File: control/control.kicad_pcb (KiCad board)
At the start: 2 copper layers, 100 x 40 mm, 63 parts, among them CON1 USB-MICRO-B, IC1 AD8542, IC2 STM32F072CBT6, IC3 ADP3335, IC4 AD8495, IC5 NCP1117, P1 SWD, P2 CONN_02X04, P3 CONN_01X02, U1 ROTENC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

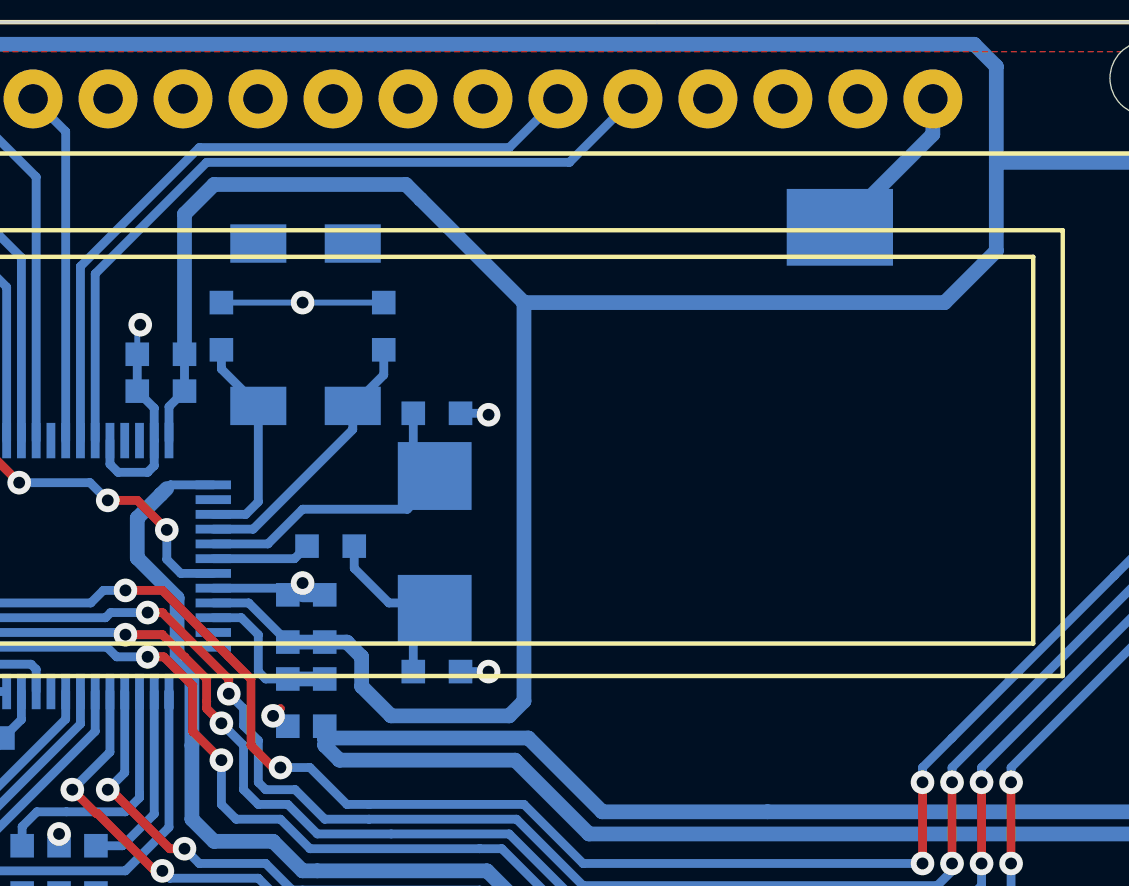
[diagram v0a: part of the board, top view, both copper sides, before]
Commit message: smaller 32k xtal, closes #21
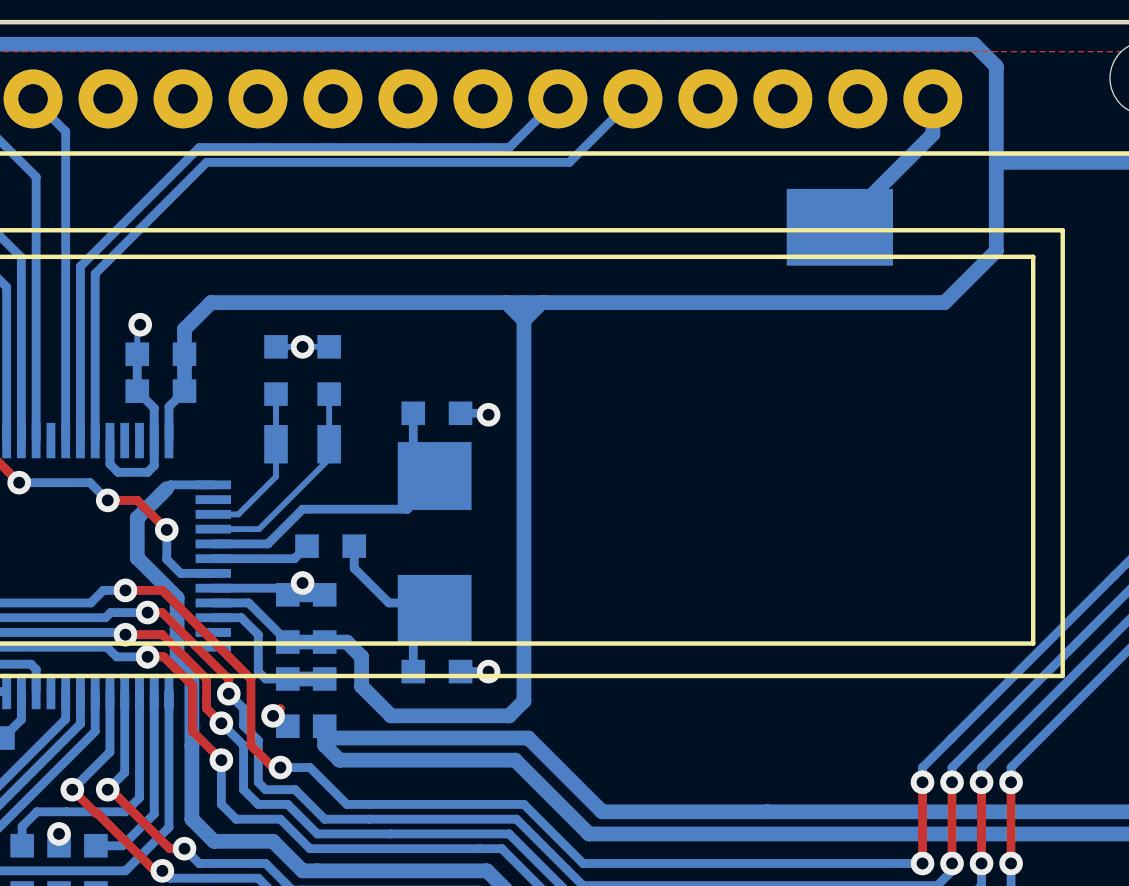
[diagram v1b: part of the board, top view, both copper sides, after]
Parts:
- X1: footprint control:SMD_XTAL_8038 -> control:R0805
- moved C11 2.38 mm to (93.1, 111.0)
- moved C12 2.38 mm to (94.9, 111.0)
- moved X1 1.43 mm to (93.1, 114.3), turned to 0 degrees
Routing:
- net VDD: track 301.8 -> 298.0 mm
- net GND: track 71.9 -> 68.2 mm
- net Net-(C12-Pad2): track 9.26 -> 7.11 mm
- net Net-(C11-Pad2): track 7.37 -> 5.45 mm

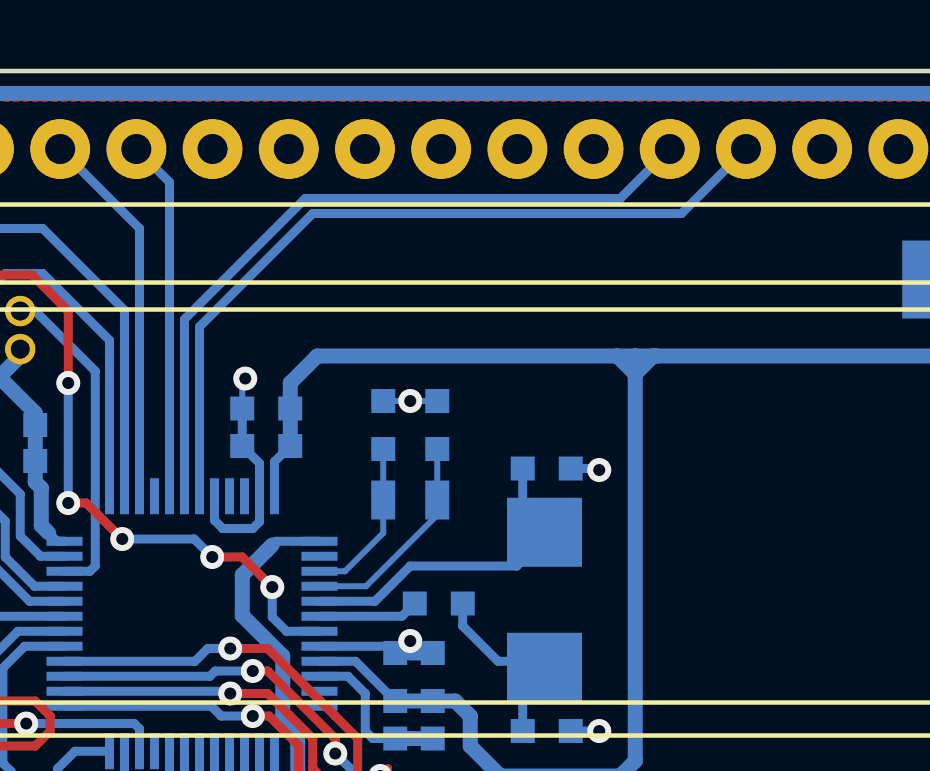
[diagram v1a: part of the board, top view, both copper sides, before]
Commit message: add LEDs to control, closes #22
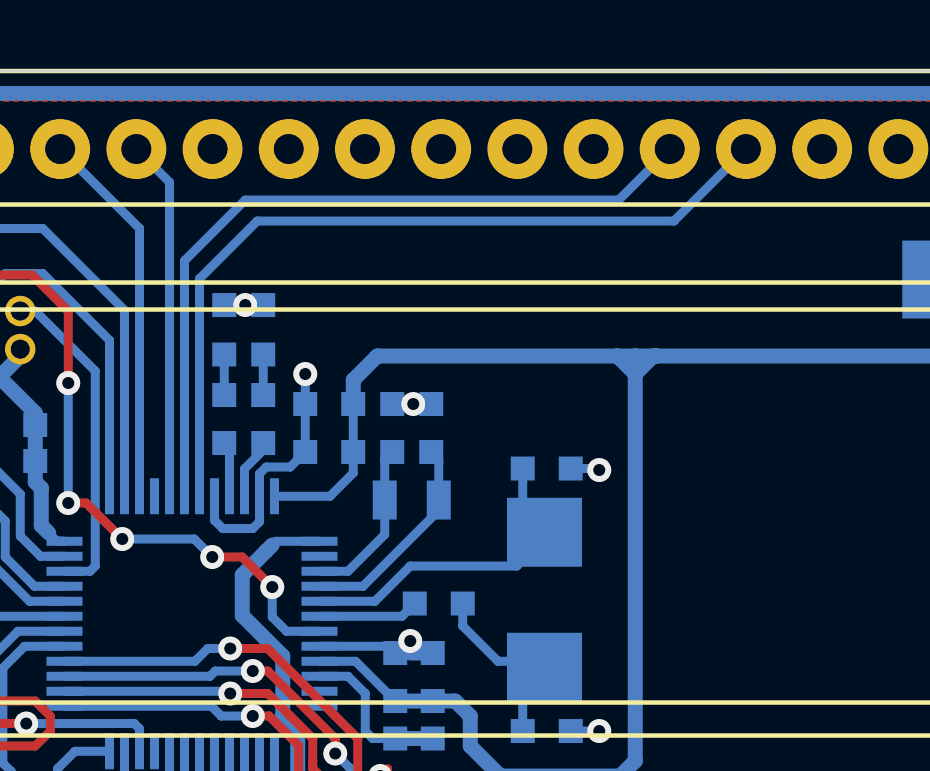
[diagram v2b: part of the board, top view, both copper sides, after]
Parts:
- added D3: GRN, control:LED0603, B.Cu at (87.8, 107.8)
- added D4: BLU, control:LED0603, B.Cu at (89.1, 107.8)
- added R13: 1k, control:R0603, B.Cu at (87.8, 110.8)
- added R14: 1k, control:R0603, B.Cu at (89.1, 110.8)
- moved C7 2.11 mm to (92.1, 112.7)
- moved C4 2.11 mm to (92.1, 111.1)
- moved C11 0.32 mm to (93.4, 111.1)
- moved C12 0.22 mm to (94.7, 111.1)
- moved X1 0.05 mm to (93.2, 114.3)
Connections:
- IC2 pad 45: (no net) -> Net-(IC2-Pad45)
- IC2 pad 46: (no net) -> Net-(IC2-Pad46)
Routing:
- net Net-(IC2-Pad46): track 0.00 -> 2.03 mm
- net Net-(IC2-Pad45): track 0.00 -> 1.85 mm
- net GND: track 68.2 -> 69.9 mm, vias 21 -> 22
- net Net-(D4-Pad2): track 0.00 -> 1.35 mm
- net Net-(D3-Pad2): track 0.00 -> 1.35 mm
- net /~OLED_CS: track 24.4 -> 25.6 mm
- net /~OLED_RST: track 26.3 -> 27.3 mm

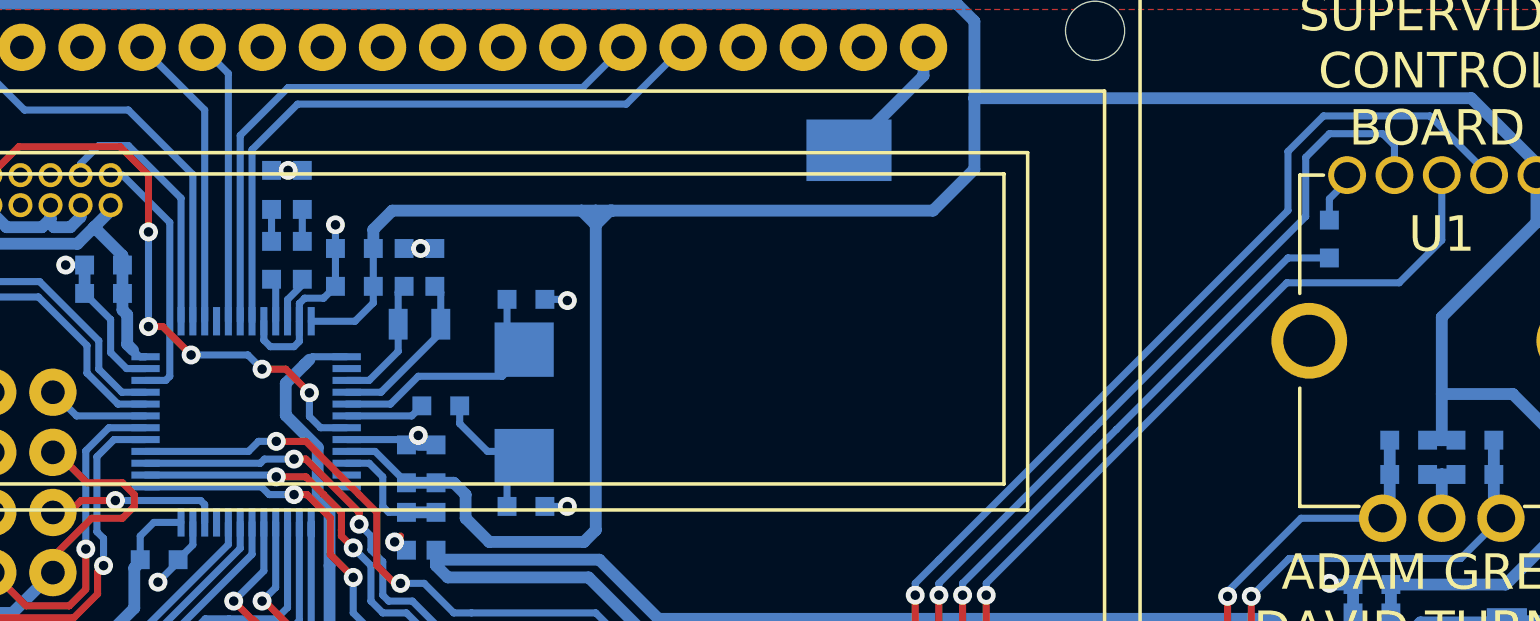
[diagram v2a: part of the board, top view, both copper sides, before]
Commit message: add more resistors to rot end LEDs
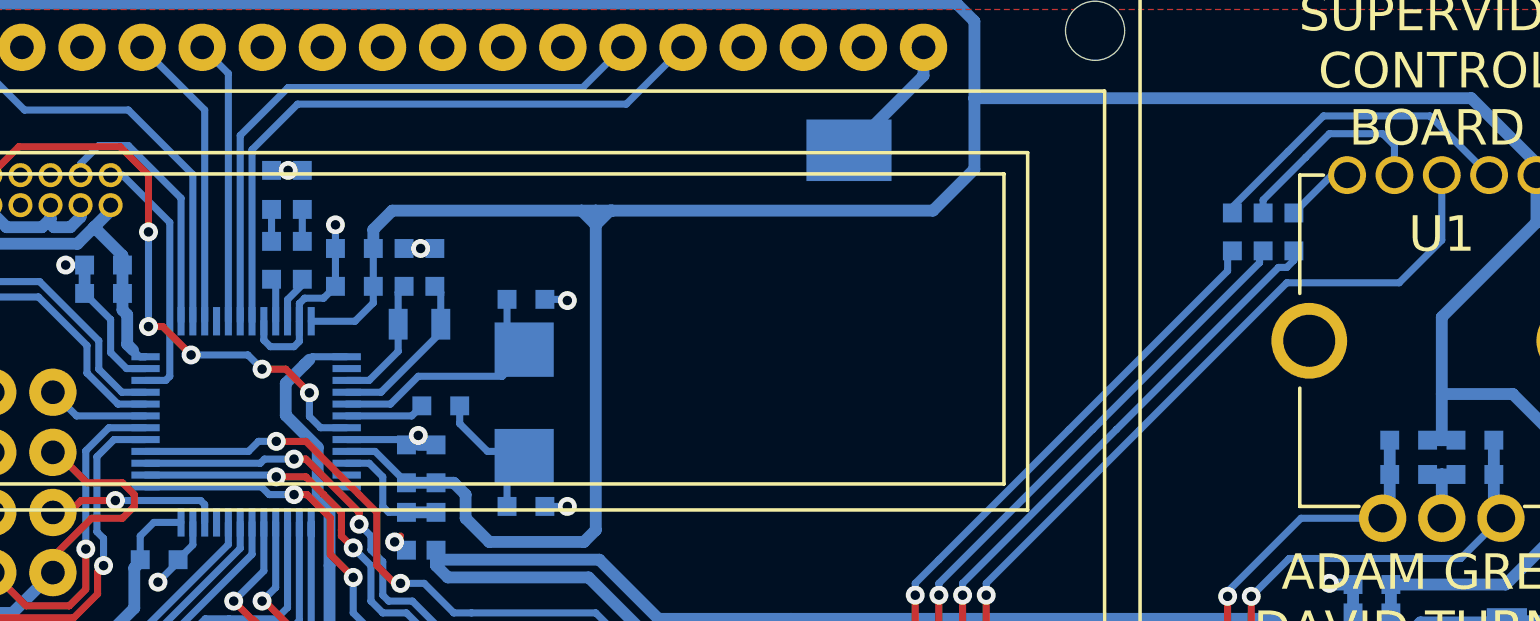
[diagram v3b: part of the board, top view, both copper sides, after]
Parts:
- added R15: 50R, control:R0603, B.Cu at (129.7, 109.6)
- added R16: 50R, control:R0603, B.Cu at (128.4, 109.6)
- moved R12 2.42 mm to (131.0, 109.6), turned to 270 degrees
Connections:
- R12 pad 1: /ENC_RED -> Net-(R12-Pad1)
- R12 pad 2: Net-(R12-Pad2) -> /ENC_RED
- U1 pad 1: Net-(R12-Pad2) -> Net-(R12-Pad1)
- U1 pad 2: /ENC_GRN -> Net-(R15-Pad1)
- U1 pad 4: /ENC_BLU -> Net-(R16-Pad1)
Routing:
- net /ENC_BLU: track 76.0 -> 60.7 mm
- net Net-(R16-Pad1): track 0.00 -> 13.7 mm
- net /ENC_GRN: track 72.6 -> 62.3 mm
- net Net-(R15-Pad1): track 0.00 -> 8.72 mm
- net Net-(R12-Pad1): track 0.00 -> 3.16 mm
- net Net-(R12-Pad2): track 2.21 -> 0.00 mm
- net /ENC_RED: track 65.4 -> 64.2 mm

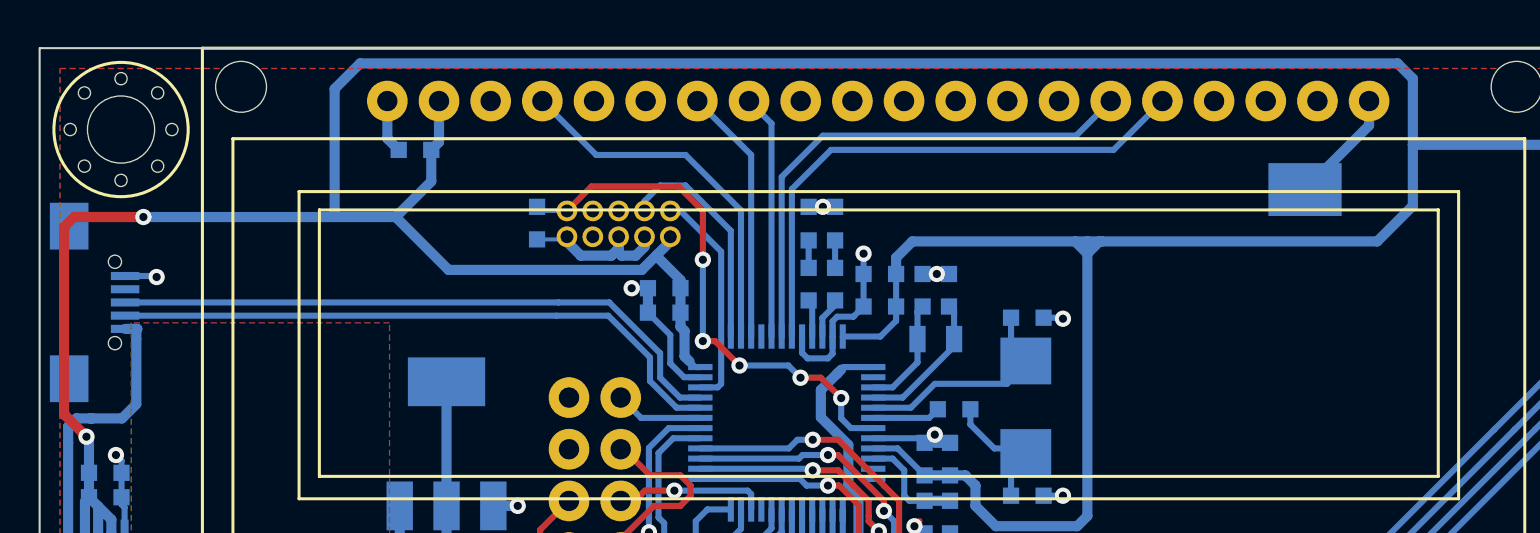
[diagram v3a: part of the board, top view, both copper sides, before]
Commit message: add tagconnect TC2030-CTX-NL footprint
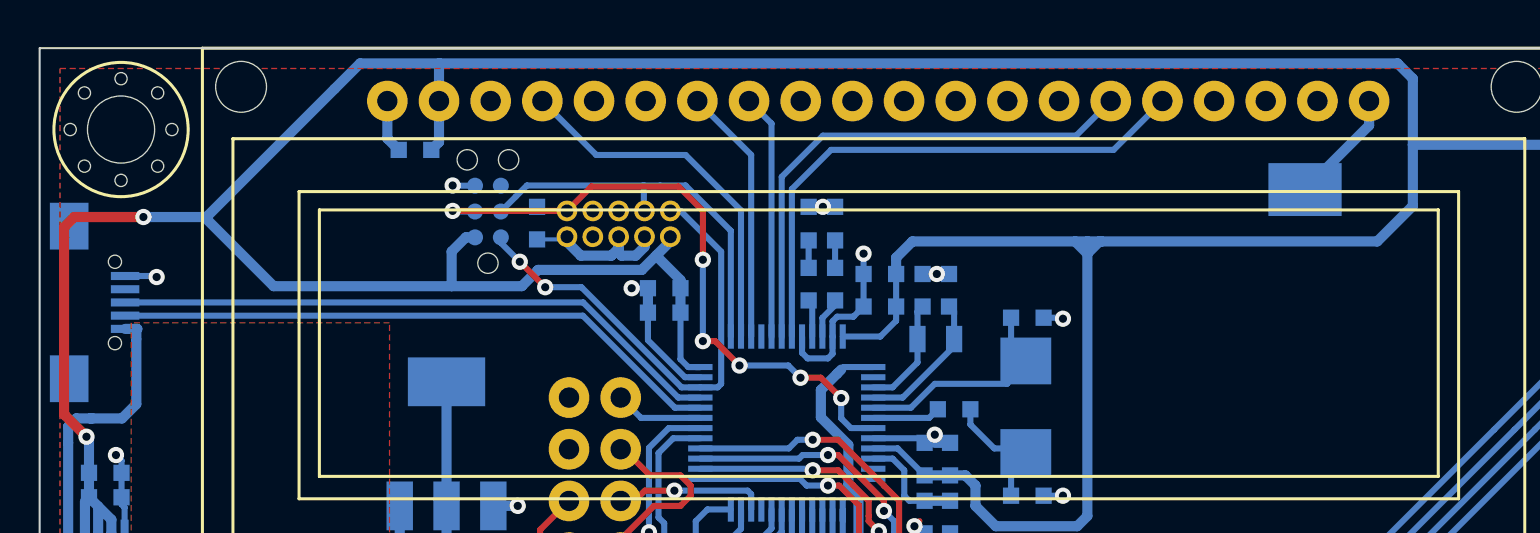
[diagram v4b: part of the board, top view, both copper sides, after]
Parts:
- added P4: CONN_02X03, control:TC2030-NL, B.Cu at (71.4, 109.3)
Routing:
- net /SWDIO: track 10.9 -> 24.2 mm, vias 0 -> 2
- net /SWDCLK: track 11.2 -> 19.2 mm
- net /nRST: track 26.4 -> 33.1 mm, vias 5 -> 6
- net VDD: track 298.0 -> 303.1 mm
- net GND: track 69.9 -> 71.0 mm, vias 22 -> 23
- net /USB_DP: track 30.9 -> 30.2 mm
- net /USB_DM: track 30.8 -> 30.1 mm

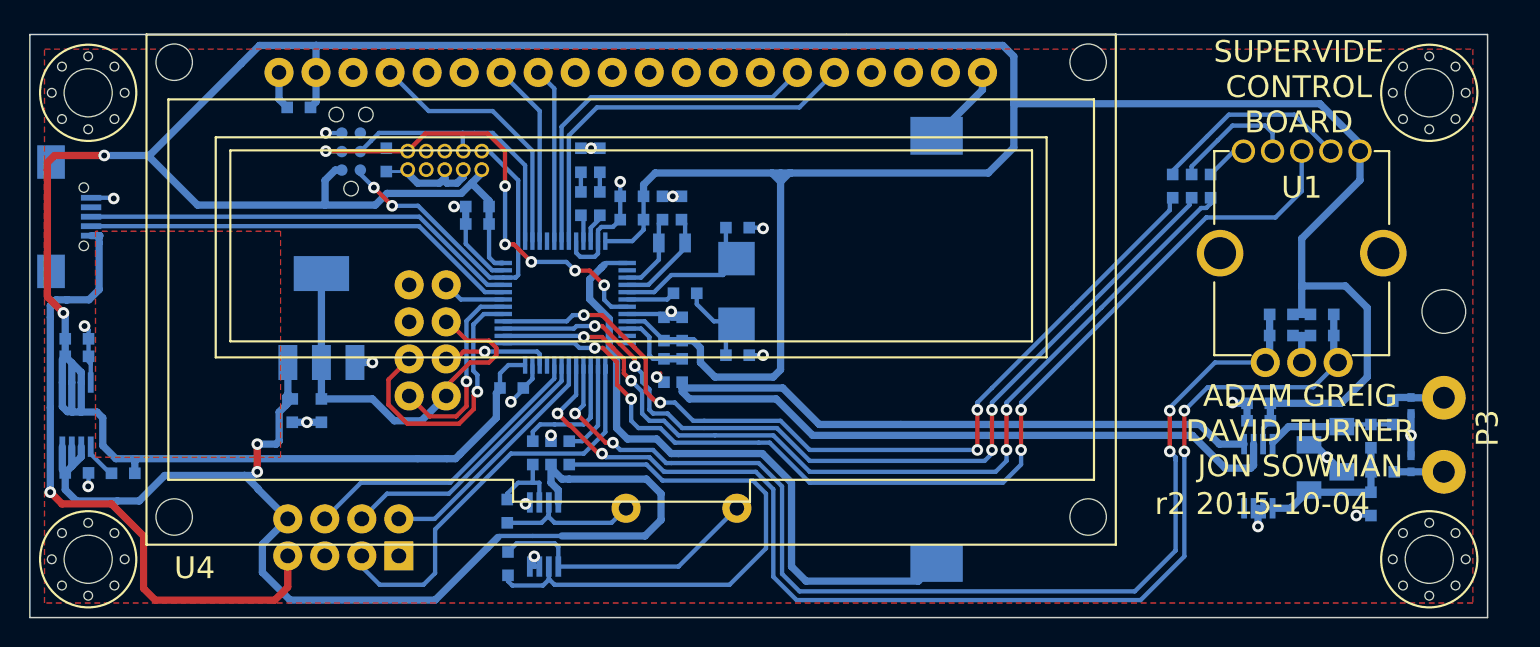
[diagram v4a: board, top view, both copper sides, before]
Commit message: rework buzzer driver to use non-inverting amplifiers
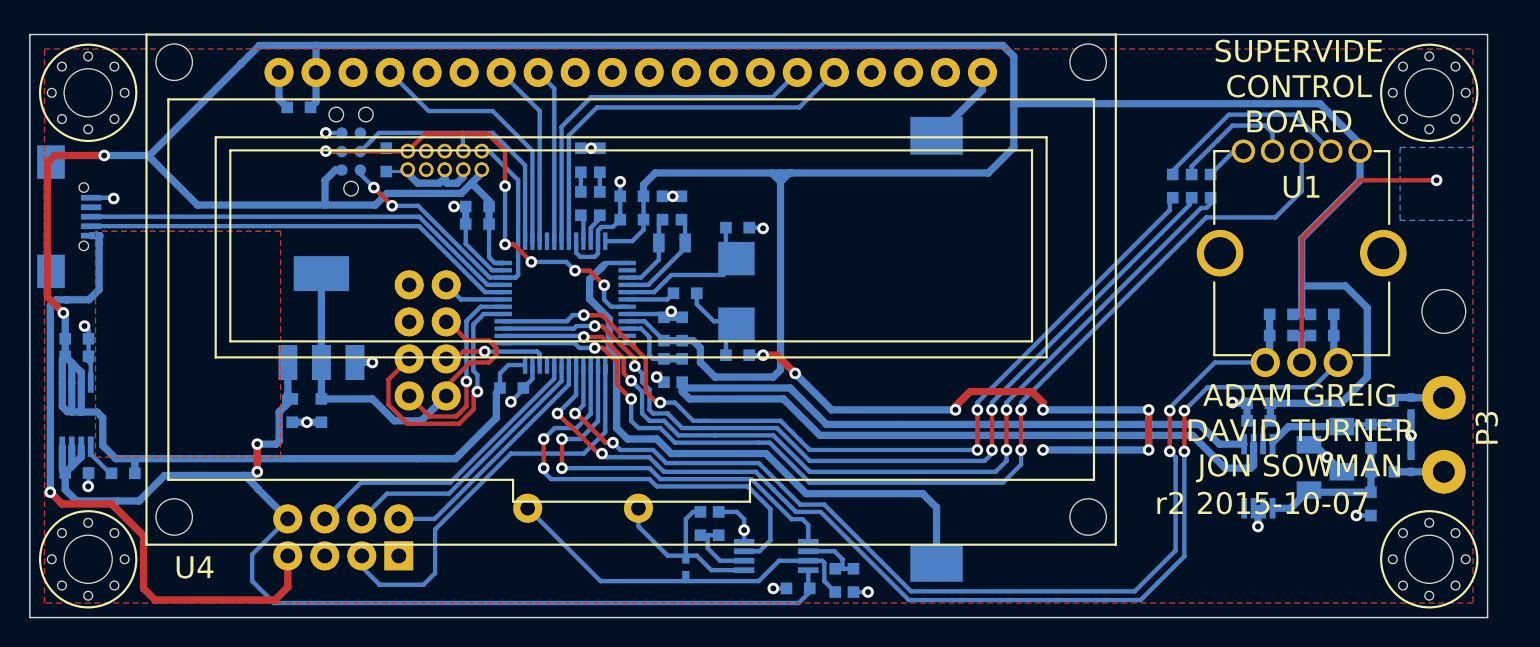
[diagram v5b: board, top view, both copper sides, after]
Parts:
- added D5: CGA0402MLC-12G, control:R0402, B.Cu at (95.0, 136.0)
- R1, R5: value 15k -> 4k7
- moved R6 23.7 mm to (106.5, 138.2)
- moved R5 23.0 mm to (105.2, 138.2)
- moved C26 19.7 mm to (103.5, 138.0), turned to 180 degrees
- moved R1 13.5 mm to (96.0, 132.8)
- moved IC1 12.8 mm to (99.0, 136.8), turned to 0 degrees
- moved R3 10.8 mm to (97.2, 132.8), turned to 270 degrees
- moved SP1 6.75 mm to (91.8, 132.5)
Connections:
- IC1 pad 3: GND -> /PIEZO_B
- IC1 pad 5: GND -> /PIEZO_A
- R3 pad 1: Net-(IC1-Pad2) -> GND
- R3 pad 2: /PIEZO_A -> Net-(IC1-Pad2)
- R6 pad 1: Net-(IC1-Pad6) -> GND
- R6 pad 2: /PIEZO_B -> Net-(IC1-Pad6)
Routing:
- net GND: track 71.0 -> 133.8 mm, vias 23 -> 30
- net Net-(IC1-Pad2): track 38.6 -> 5.00 mm
- net /PIEZO_A: track 6.57 -> 28.5 mm, vias 0 -> 2
- net /PIEZO_B: track 8.63 -> 30.4 mm, vias 0 -> 2
- net Net-(D5-Pad2): track 10.8 -> 25.8 mm
- net Net-(D5-Pad1): track 19.1 -> 14.1 mm
- net /ENC_B: track 82.5 -> 79.0 mm
- net /ENC_A: track 75.7 -> 72.2 mm
- net Net-(BT1-Pad1): track 44.5 -> 42.3 mm
- net VCC: track 84.4 -> 82.6 mm
- net Net-(IC1-Pad6): track 5.51 -> 4.48 mm
- added copper zone on B.Cu, net GND
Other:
- board text added: "USE CR2032"
- board text added: "r2 2015-10-07"
- board text removed: "r2 2015-10-04"
